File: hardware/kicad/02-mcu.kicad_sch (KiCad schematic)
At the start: 6 parts, among them U1 ESP32-S3-N16R8

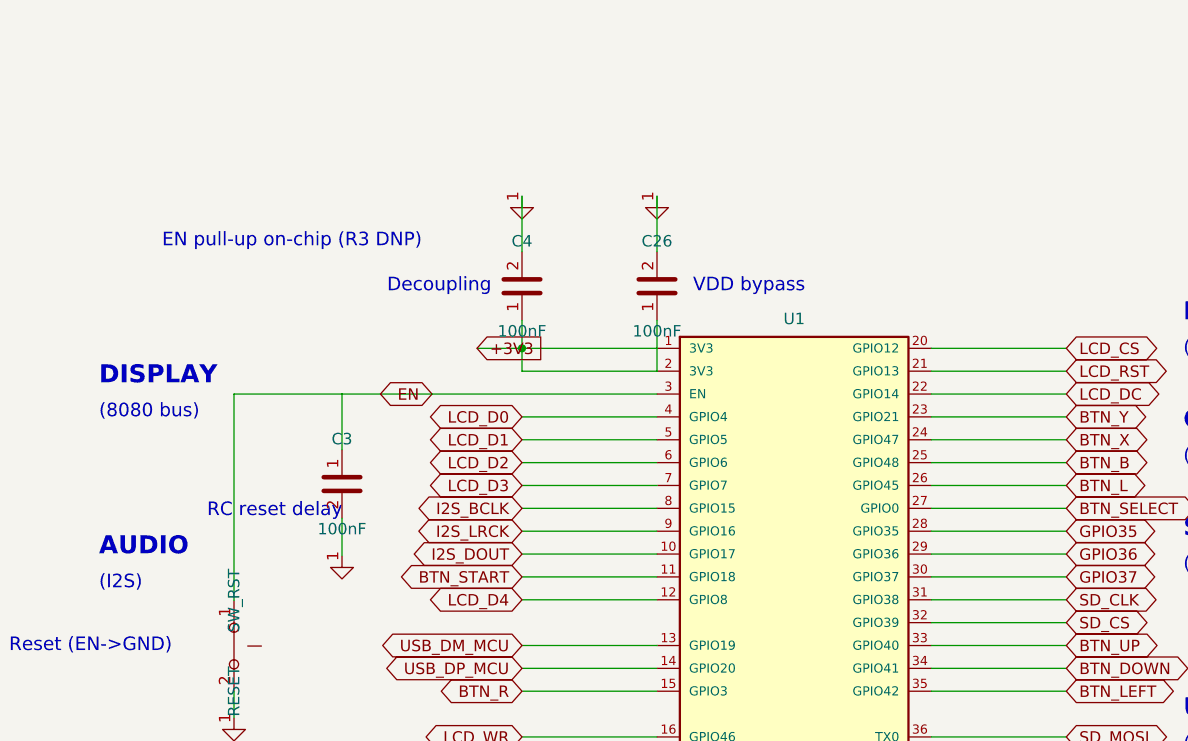
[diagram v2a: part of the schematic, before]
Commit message: sch(EN): stop drawing an RC that the board does not have — v1 as-built, v2 fixed
v1 is not being re-fabricated, so the missing EN network is recorded as
an as-built limitation and the schematic is corrected to match copper,
rather than the board being patched.

What the datasheet actually says, page 28, under the peripheral
reference schematic: an RC delay circuit MUST be added at the EN pin,
R = 10k and C = 1uF typical, and figure 7 draws R7 from VDD33 to EN with
C8 0.1uF from EN to GND. The v1 board has NEITHER — R3 is DNP and C3 is
wired as a second decoupling cap, so EN reaches only U1.3 and SW_RST
pad 1.

It survived behind two sentences nobody checked against copper: mcu.py
claimed "the module integrates a 10k EN pull-up on-module (per Espressif
reference design), so an external pull-up is redundant", which is false,
and hardware-audit-bugs.md asserts "EN RC delay (R3+C3) intact" twice.
Same class as the R25 finding that a justification comment can outrank
the datasheet.

Not patched on v1 because the only cap available sits 28mm away, and
dragging EN that far would trade a missing RC for a long high-impedance
antenna on the reset line — worse than bare. The board boots today; this
is a margin defect (slow ramps, brown-out), not a dead board.

C3 is therefore drawn where the board has it: the third cap in the
decoupling row, pad 1 on +3V3, twin of C4 — routing.py has called it
"ESP32 decoupling 1" all along. Placed right of C26 rather than at the
symmetric slot left of C4, which is occupied by C4's own caption; the
overlap gate caught both that and the annotation running across the
capacitor references.

  verify_netlist_diff  T4   1 mismatch -> 0            PASS
  verify_schematic_pin_connectivity  338 pins, 0 floating  PASS
  verify_schematic_overlaps / crossings / erc / pcb_sync  PASS

Hardware gates: 1 of 6 red. Only verify_cpl_rotation_law is left, on U2
and J4, and it stays red until the visual check.

v2 requirement recorded in docs/known-issues.md: 10k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
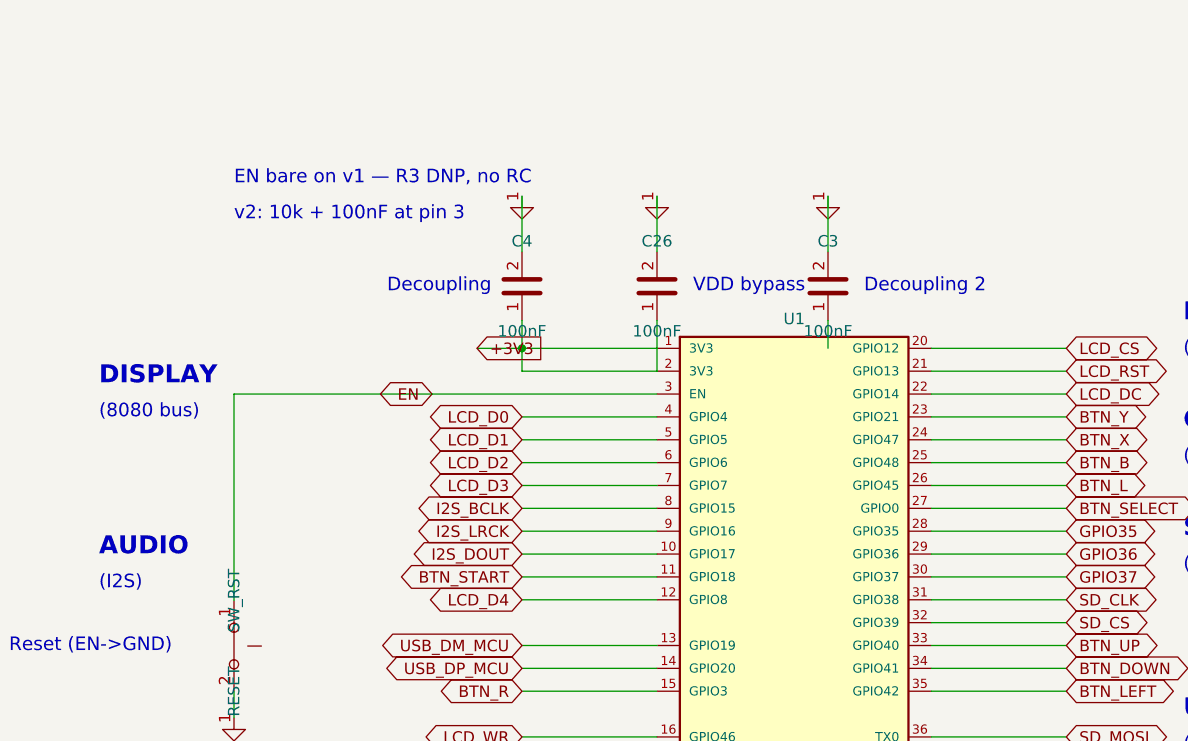
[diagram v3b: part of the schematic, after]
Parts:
- C4: renamed from SW_BOOT; value BOOT -> 100nF; symbol SW_Push -> C
- SW_BOOT: renamed from SW_RST; value RESET -> BOOT
- SW_RST: renamed from C3; value 100nF -> RESET; symbol C -> SW_Push
- renumbered C4 to C3
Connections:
- net +3V3: now also C4.1; no longer C3.1
- net BTN_SELECT: now also SW_BOOT.1; no longer C4.1
- net EN: no longer SW_BOOT.1
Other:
- note added: "Decoupling 2"
- note added: "EN bare on v1 — R3 DNP, no RC"
- note added: "v2: 10k + 100nF at pin 3"
- note removed: "EN pull-up on-chip (R3 DNP)"
- note removed: "RC reset delay"
- moved on the sheet: C3, SW_BOOT
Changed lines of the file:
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@@
   (wire (pts (xy 184.76 136.98) (xy 159.76 136.98)) (stroke (width 0) (type default)))
   (global_label "EN" (shape bidirectional) (at 159.76 136.98 180) (effects (font (size 1.27 1.27))) (property "Intersheetrefs" "" (at 0 0 0) (effects (font (size 1.27 1.27)) hide)))
-  (text "EN pull-up on-chip (R3 DNP)" (at 129.76 120 0) (effects (font (size 1.5 1.5)) (justify left)))
-  (symbol (lib_id "C") (at 149.76 146.98 0) (unit 1) (exclude_from_sim no) (in_bom yes) (on_board yes) (dnp no) (property "Reference" "C3" (at 149.76 141.98 0) (effects (font (size 1.27 1.27)))) (property "Value" "100nF" (at 149.76 151.98 0) (effects (font (size 1.27 1.27)))) (pin "1") (pin "2") (instances (project "esp32-emu-turbo" (path "/00000003-cafe-4000-8000-000000000003" (reference "C3") (unit 1)))))
-  (wire (pts (xy 159.76 136.98) (xy 149.76 136.98)) (stroke (width 0) (type default)))
-  (wire (pts (xy 149.76 136.98) (xy 149.76 143.17)) (stroke (width 0) (type default)))
-  (symbol (lib_id "GND") (at 149.76 154.98 0) (unit 1) (exclude_from_sim no) (in_bom no) (on_board no) (dnp no) (property "Reference" "#PWR001" (at 149.76 152.98 0) (effects (font (size 1.27 1.27)) hide)) (property "Value" "GND" (at 149.76 156.98 0) (effects (font (size 1.27 1.27)) hide)) (pin "1") (instances (project "esp32-emu-turbo" (path "/00000003-cafe-4000-8000-000000000003" (reference "#PWR001") (unit 1)))))
-  (wire (pts (xy 149.76 150.79) (xy 149.76 154.98)) (stroke (width 0) (type default)))
-  (text "RC reset delay" (at 134.76 149.98 0) (effects (font (size 1.5 1.5)) (justify left)))
+  (text "EN bare on v1 — R3 DNP, no RC" (at 137.76 113 0) (effects (font (size 1.5 1.5)) (justify left)))
+  (text "v2: 10k + 100nF at pin 3" (at 137.76 117 0) (effects (font (size 1.5 1.5)) (justify left)))
   (symbol (lib_id "SW_Push") (at 137.76 164.98 270) (unit 1) (exclude_from_sim no) (in_bom yes) (on_board yes) (dnp no) (property "Reference" "SW_RST" (at 137.76 159.932 0) (effects (font (size 1.27 1.27)))) (property "Value" "RESET" (at 137.76 170.028 0) (effects (font (size 1.27 1.27)))) (pin "1") (pin "2") (instances (project "esp32-emu-turbo" (path "/00000003-cafe-4000-8000-000000000003" (reference "SW_RST") (unit 1)))))
   (wire (pts (xy 137.76 159.89999999999998) (xy 137.76 136.98)) (stroke (width 0) (type default)))
-  (wire (pts (xy 137.76 136.98) (xy 149.76 136.98)) (stroke (width 0) (type default)))
-  (symbol (lib_id "GND") (at 137.76 172.98 0) (unit 1) (exclude_from_sim no) (in_bom no) (on_board no) (dnp no) (property "Reference" "#PWR002" (at 137.76 170.98 0) (effects (font (size 1.27 1.27)) hide)) (property "Value" "GND" (at 137.76 174.98 0) (effects (font (size 1.27 1.27)) hide)) (pin "1") (instances (project "esp32-emu-turbo" (path "/00000003-cafe-4000-8000-000000000003" (reference "#PWR002") (unit 1)))))
+  (wire (pts (xy 159.76 136.98) (xy 137.76 136.98)) (stroke (width 0) (type default)))
+  (symbol (lib_id "GND") (at 137.76 172.98 0) (unit 1) (exclude_from_sim no) (in_bom no) (on_board no) (dnp no) (property "Reference" "#PWR001" (at 137.76 170.98 0) (effects (font (size 1.27 1.27)) hide)) (property "Value" "GND" (at 137.76 174.98 0) (effects (font (size 1.27 1.27)) hide)) (pin "1") (instances (project "esp32-emu-turbo" (path "/00000003-cafe-4000-8000-000000000003" (reference "#PWR001") (unit 1)))))
   (wire (pts (xy 137.76 170.06) (xy 137.76 172.98)) (stroke (width 0) (type default)))
   (text "Reset (EN->GND)" (at 112.75999999999999 164.98 0) (effects (font (size 1.5 1.5)) (justify left)))
@@
   (global_label "BTN_SELECT" (shape bidirectional) (at 119.75999999999999 193.98 0) (effects (font (size 1.27 1.27))) (property "Intersheetrefs" "" (at 0 0 0) (effects (font (size 1.27 1.27)) hide)))
   (wire (pts (xy 119.75999999999999 196.89999999999998) (xy 119.75999999999999 193.98)) (stroke (width 0) (type default)))
-  (symbol (lib_id "GND") (at 119.75999999999999 209.98 0) (unit 1) (exclude_from_sim no) (in_bom no) (on_board no) (dnp no) (property "Reference" "#PWR003" (at 119.75999999999999 207.98 0) (effects (font (size 1.27 1.27)) hide)) (property "Value" "GND" (at 119.75999999999999 211.98 0) (effects (font (size 1.27 1.27)) hide)) (pin "1") (instances (project "esp32-emu-turbo" (path "/00000003-cafe-4000-8000-000000000003" (reference "#PWR003") (unit 1)))))
+  (symbol (lib_id "GND") (at 119.75999999999999 209.98 0) (unit 1) (exclude_from_sim no) (in_bom no) (on_board no) (dnp no) (property "Reference" "#PWR002" (at 119.75999999999999 207.98 0) (effects (font (size 1.27 1.27)) hide)) (property "Value" "GND" (at 119.75999999999999 211.98 0) (effects (font (size 1.27 1.27)) hide)) (pin "1") (instances (project "esp32-emu-turbo" (path "/00000003-cafe-4000-8000-000000000003" (reference "#PWR002") (unit 1)))))
   (wire (pts (xy 119.75999999999999 207.06) (xy 119.75999999999999 209.98)) (stroke (width 0) (type default)))
   (text "BOOT (GPIO0->GND)" (at 104.75999999999999 214.98 0) (effects (font (size 1.5 1.5)) (justify left)))
@@
   (wire (pts (xy 169.76 128.81) (xy 169.76 131.9)) (stroke (width 0) (type default)))
   (junction (at 169.76 131.9) (diameter 0) (color 0 0 0 0))
-  (symbol (lib_id "GND") (at 169.76 115 0) (unit 1) (exclude_from_sim no) (in_bom no) (on_board no) (dnp no) (property "Reference" "#PWR004" (at 169.76 113 0) (effects (font (size 1.27 1.27)) hide)) (property "Value" "GND" (at 169.76 117 0) (effects (font (size 1.27 1.27)) hide)) (pin "1") (instances (project "esp32-emu-turbo" (path "/00000003-cafe-4000-8000-000000000003" (reference "#PWR004") (unit 1)))))
+  (symbol (lib_id "GND") (at 169.76 115 0) (unit 1) (exclude_from_sim no) (in_bom no) (on_board no) (dnp no) (property "Reference" "#PWR003" (at 169.76 113 0) (effects (font (size 1.27 1.27)) hide)) (property "Value" "GND" (at 169.76 117 0) (effects (font (size 1.27 1.27)) hide)) (pin "1") (instances (project "esp32-emu-turbo" (path "/00000003-cafe-4000-8000-000000000003" (reference "#PWR003") (unit 1)))))
   (wire (pts (xy 169.76 121.19) (xy 169.76 115)) (stroke (width 0) (type default)))
   (text "Decoupling" (at 154.76 125 0) (effects (font (size 1.5 1.5)) (justify left)))
+  (symbol (lib_id "C") (at 203.76 125 180) (unit 1) (exclude_from_sim no) (in_bom yes) (on_board yes) (dnp no) (property "Reference" "C3" (at 203.76 120.0 0) (effects (font (size 1.27 1.27)))) (property "Value" "100nF" (at 203.76 130.0 0) (effects (font (size 1.27 1.27)))) (pin "1") (pin "2") (instances (project "esp32-emu-turbo" (path "/00000003-cafe-4000-8000-000000000003" (reference "C3") (unit 1)))))
+  (wire (pts (xy 203.76 128.81) (xy 203.76 131.9)) (stroke (width 0) (type default)))
+  (symbol (lib_id "GND") (at 203.76 115 0) (unit 1) (exclude_from_sim no) (in_bom no) (on_board no) (dnp no) (property "Reference" "#PWR004" (at 203.76 113 0) (effects (font (size 1.27 1.27)) hide)) (property "Value" "GND" (at 203.76 117 0) (effects (font (size 1.27 1.27)) hide)) (pin "1") (instances (project "esp32-emu-turbo" (path "/00000003-cafe-4000-8000-000000000003" (reference "#PWR004") (unit 1)))))
+  (wire (pts (xy 203.76 121.19) (xy 203.76 115)) (stroke (width 0) (type default)))
+  (text "Decoupling 2" (at 207.76 125 0) (effects (font (size 1.5 1.5)) (justify left)))
   (symbol (lib_id "C") (at 184.76 125 180) (unit 1) (exclude_from_sim no) (in_bom yes) (on_board yes) (dnp no) (property "Reference" "C26" (at 184.76 120.0 0) (effects (font (size 1.27 1.27)))) (property "Value" "100nF" (at 184.76 130.0 0) (effects (font (size 1.27 1.27)))) (pin "1") (pin "2") (instances (project "esp32-emu-turbo" (path "/00000003-cafe-4000-8000-000000000003" (reference "C26") (unit 1)))))
   (wire (pts (xy 184.76 128.81) (xy 184.76 134.44)) (stroke (width 0) (type default)))
